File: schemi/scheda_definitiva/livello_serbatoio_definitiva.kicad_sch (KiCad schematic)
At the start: 47 parts

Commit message: modifiche scheda definitiva (rev. C)
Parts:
- removed D3: (no value), symbol Device:D
- removed J2, J4: (no value), symbol Connector:Screw_Terminal_01x04
- removed R11: (no value), symbol Device:R
- added J8: Ext_connections, TerminalBlock_RND:TerminalBlock_RND_205-00051_1x08_P5.00mm_Horizontal, symbol Connector:Screw_Terminal_01x08
- added R5: 10k, Resistor_THT:R_Axial_DIN0309_L9.0mm_D3.2mm_P12.70mm_Horizontal, symbol Device:R
- C1, C2, C3, C4, C5, C6: value (none) -> 100nF; footprint (none) -> Capacitor_THT:C_Disc_D5.0mm_W2.5mm_P2.50mm
- C7, C8: value (none) -> 22pF; footprint (none) -> Capacitor_THT:C_Disc_D5.0mm_W2.5mm_P2.50mm
- C9: value (none) -> 100uF; footprint (none) -> Capacitor_THT:CP_Radial_D5.0mm_P2.00mm
- D1: value (none) -> LED_TX; footprint (none) -> LED_THT:LED_D5.0mm
- D2: value (none) -> LED_RX; footprint (none) -> LED_THT:LED_D5.0mm
- D4: value (none) -> LED_ON; footprint (none) -> LED_THT:LED_D5.0mm
- F1: value (none) -> MF-MSMF050-2; footprint (none) -> simboli_custom:MF-MSMF_1812_4532Metric_Pad1.30x3.40mm_HandSolder
- FB1: value (none) -> MPZ2012; footprint (none) -> Inductor_SMD:L_0805_2012Metric_Pad1.15x1.40mm_HandSolder
- H1: value (none) -> HOLE1; footprint (none) -> MountingHole:MountingHole_3mm_Pad_Via
- H2: value (none) -> HOLE2; footprint (none) -> MountingHole:MountingHole_3mm_Pad_Via
- H3: value (none) -> HOLE3; footprint (none) -> MountingHole:MountingHole_3mm_Pad_Via
- H4: value (none) -> HOLE4; footprint (none) -> MountingHole:MountingHole_3mm_Pad_Via
- J1: value (none) -> USB_B; footprint (none) -> simboli_custom:USB_B_OST_USB-B1HSxx_Horizontal
- J3: value (none) -> CONN_LCD; footprint (none) -> Connector_PinSocket_2.54mm:PinSocket_1x16_P2.54mm_Vertical
- J5: value (none) -> ICSP; footprint (none) -> Connector_PinHeader_2.54mm:PinHeader_2x03_P2.54mm_Vertical
- J6: value (none) -> Exp_Analog_2; footprint (none) -> Connector_PinSocket_2.54mm:PinSocket_1x04_P2.54mm_Vertical
- J7: value (none) -> Exp_Analog; footprint (none) -> Connector_PinSocket_2.54mm:PinSocket_1x05_P2.54mm_Vertical
- JP1: value (none) -> A0J; footprint (none) -> Jumper:SolderJumper-2_P1.3mm_Open_Pad1.0x1.5mm
- JP2: value (none) -> A1J; footprint (none) -> Jumper:SolderJumper-2_P1.3mm_Open_Pad1.0x1.5mm
- JP3: value (none) -> A2J; footprint (none) -> Jumper:SolderJumper-2_P1.3mm_Open_Pad1.0x1.5mm
- JP4: value (none) -> A3J; footprint (none) -> Jumper:SolderJumper-2_P1.3mm_Open_Pad1.0x1.5mm
- R1, R2, R3, R4, R9: value (none) -> 1k; footprint (none) -> Resistor_THT:R_Axial_DIN0309_L9.0mm_D3.2mm_P12.70mm_Horizontal
- R6: value (none) -> 10k; footprint (none) -> Resistor_THT:R_Axial_DIN0309_L9.0mm_D3.2mm_P12.70mm_Horizontal
- R7: value (none) -> 1M; footprint (none) -> Resistor_THT:R_Axial_DIN0309_L9.0mm_D3.2mm_P12.70mm_Horizontal
- R8: value (none) -> 330; footprint (none) -> Resistor_THT:R_Axial_DIN0309_L9.0mm_D3.2mm_P12.70mm_Horizontal
- RV1: value (none) -> POT_LCDC; footprint (none) -> simboli_custom:Trimmer_ACP_470
- SW1: value (none) -> SW_RST; footprint (none) -> Button_Switch_THT:SW_PUSH_6mm_H5mm
- TP1: value (none) -> RTS_pad; footprint (none) -> TestPoint:TestPoint_Pad_D1.0mm
- TP2: value (none) -> CTS_pad; footprint (none) -> TestPoint:TestPoint_Pad_D1.0mm
- U1: value (none) -> FT232RL; footprint (none) -> Package_SO:SSOP-28_5.3x10.2mm_P0.65mm
- U2: value (none) -> ATmega328P-PU; footprint (none) -> Package_DIP:DIP-28_W7.62mm
- U3: value (none) -> USBLC6-2SC6; footprint (none) -> Package_TO_SOT_SMD:SOT-23-6_Handsoldering
- Y1: value (none) -> 16MHz; footprint (none) -> simboli_custom:Crystal_TH_AS16_5mm
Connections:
- net D11: now also J8.3 (Pin_3)
- net D12: now also J8.4 (Pin_4)
- net D2: now also J8.8 (Pin_8), R5.1
- net GND: now also J8.2 (Pin_2), J8.5 (Pin_5), R5.2
- net VCC: now also J8.1 (Pin_1), J8.7 (Pin_7)
- net at R8.2: now also J8.6 (Pin_6)
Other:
- moved on the sheet: R8

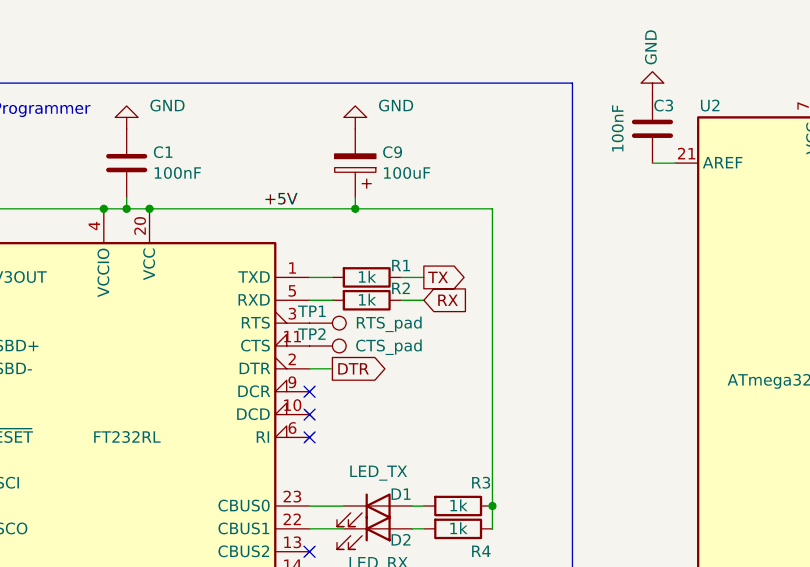
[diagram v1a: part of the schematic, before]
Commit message: scheda rev.D - rimosse resistenze RX/TX seriale - aggiustamento label
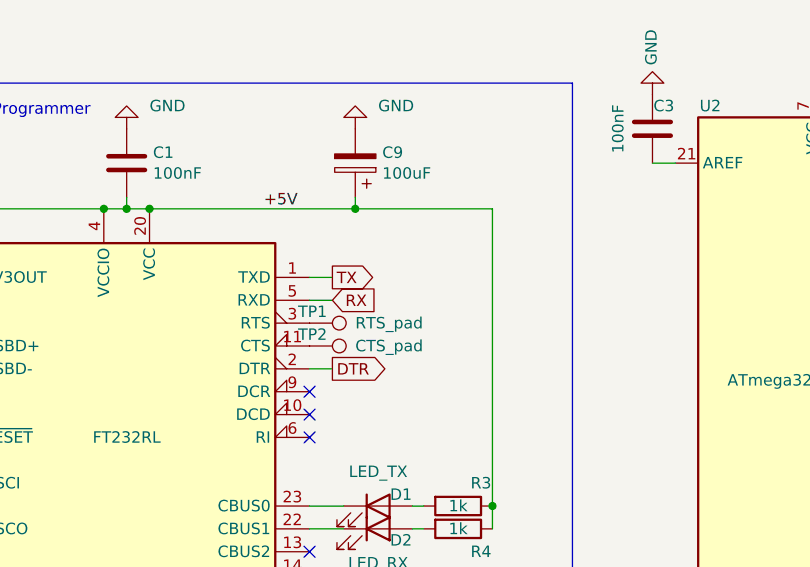
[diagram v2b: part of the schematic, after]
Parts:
- removed R1, R2: 1k, Resistor_THT:R_Axial_DIN0309_L9.0mm_D3.2mm_P12.70mm_Horizontal, symbol Device:R
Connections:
- net RX: now also U1.5 (RXD)
- net TX: now also U1.1 (TXD)

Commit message: corretto schema (placing fuse e condensatori filtro)
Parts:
- removed FB1: MPZ2012, Inductor_SMD:L_0805_2012Metric_Pad1.15x1.40mm_HandSolder, symbol Device:Ferrite_Bead
- removed R7: 1M, Resistor_THT:R_Axial_DIN0309_L9.0mm_D3.2mm_P12.70mm_Horizontal, symbol Device:R
- R9: value 1k -> 5k
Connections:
- net VCC: now also C5.2, U3.5 (VBUS)
- net at J1.1 (VBUS): now also F1.2
- removed net VBUS: C5.2, F1.2, U3.5 (VBUS)
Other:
- moved on the sheet: F1
